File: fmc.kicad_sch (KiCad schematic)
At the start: 2 parts, among them P1 ASP-134604-01, P2 ASP-134604-01

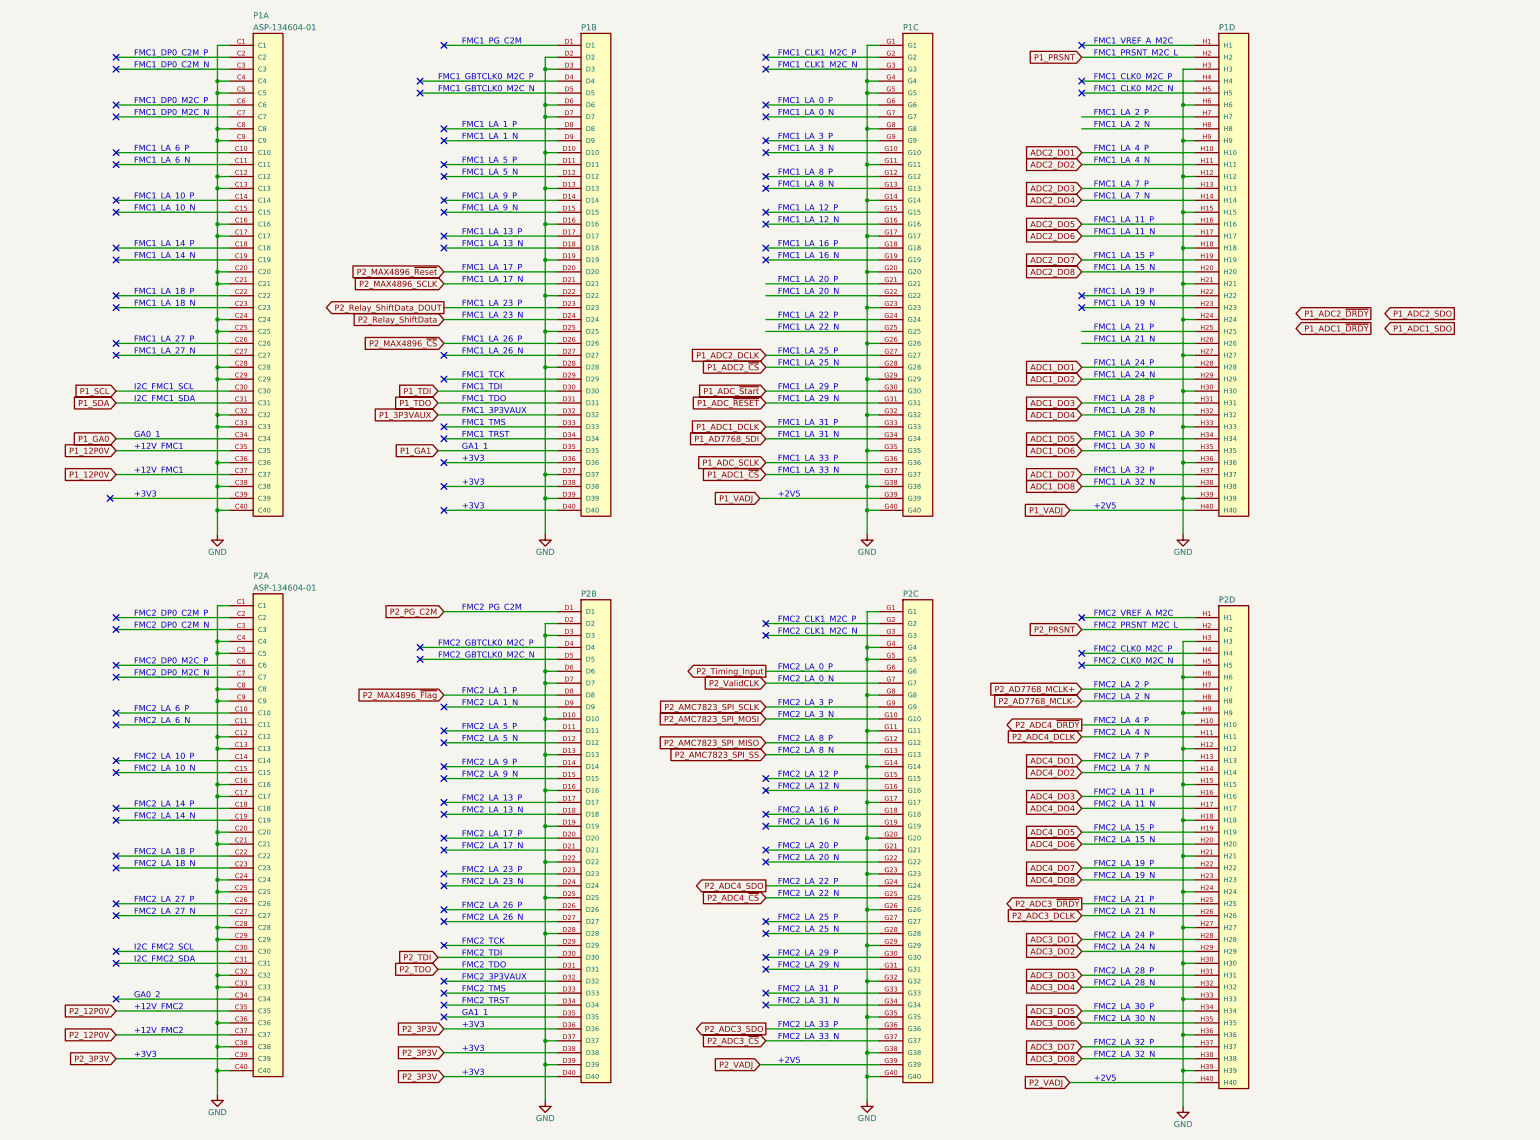
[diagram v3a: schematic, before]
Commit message: Updated Project
Schematics:
-updated level shifting IC's
-Add notes to level shifters
-Changed Relay Coil Driver channel mapping
-Added additional Mounting Hole

Layout
-WIP To Complete:
-Relay Driver ICs
- Reworking LT8582 area
- Level Shifters
- Housekeeping ICs
-Misc. error cleanup
- Silkscreen adjust
- Add Silkscreen SN & logo
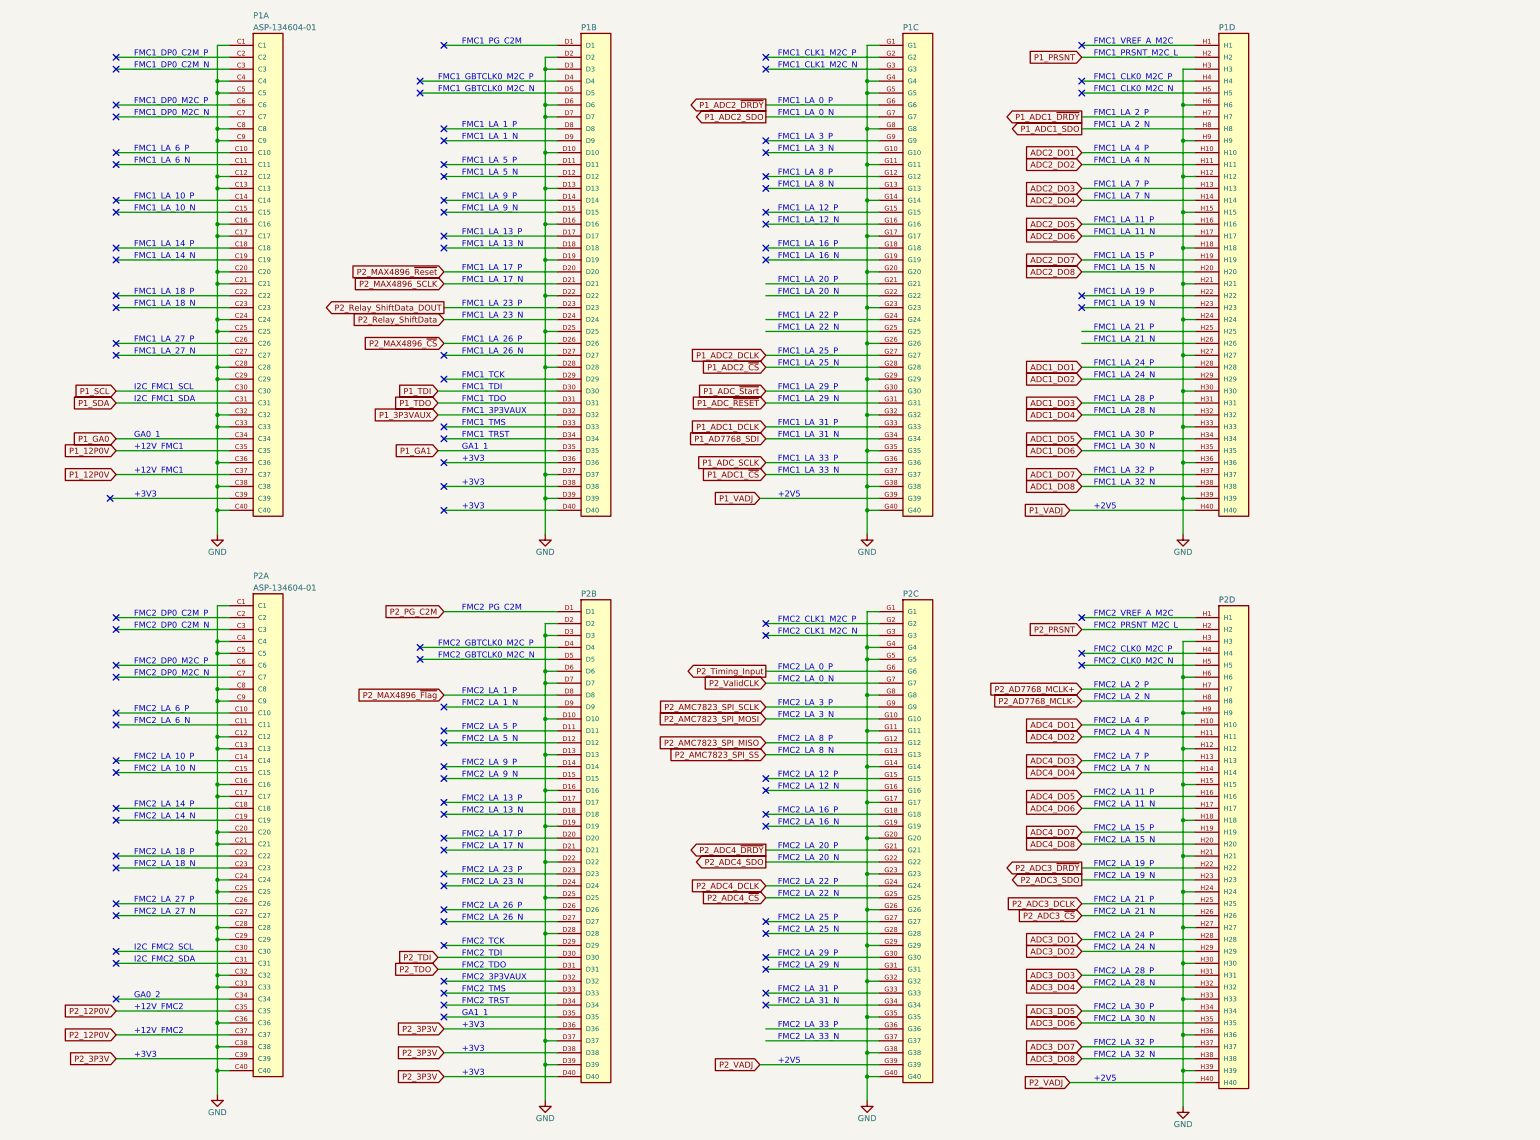
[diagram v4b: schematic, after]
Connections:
- net ADC4_DO1: now also P2.H10; no longer P2.H13
- net ADC4_DO2: now also P2.H11; no longer P2.H14
- net ADC4_DO3: now also P2.H13; no longer P2.H16
- net ADC4_DO4: now also P2.H14; no longer P2.H17
- net ADC4_DO5: now also P2.H16; no longer P2.H19
- net ADC4_DO6: now also P2.H17; no longer P2.H20
- net ADC4_DO7: now also P2.H19; no longer P2.H22
- net ADC4_DO8: now also P2.H20; no longer P2.H23
- net P1_ADC1_SDO: now also P1.H8
- net P1_ADC1_~{DRDY}: now also P1.H7
- net P1_ADC2_SDO: now also P1.G7
- net P1_ADC2_~{DRDY}: now also P1.G6
- net P2_ADC3_DCLK: now also P2.H25; no longer P2.H26
- net P2_ADC3_SDO: now also P2.H23; no longer P2.G36
- net P2_ADC3_~{CS}: now also P2.H26; no longer P2.G37
- net P2_ADC3_~{DRDY}: now also P2.H22; no longer P2.H25
- net P2_ADC4_DCLK: now also P2.G24; no longer P2.H11
- net P2_ADC4_SDO: now also P2.G22; no longer P2.G24
- net P2_ADC4_~{DRDY}: now also P2.G21; no longer P2.H10
- no-connect marks 104 -> 100
